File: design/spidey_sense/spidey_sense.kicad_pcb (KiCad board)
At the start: 2 copper layers, 63.5 x 46.5 mm, 14 parts, among them J1 Input_Screw_Terminal, J10 Output_Screw_Terminal, J2 Thermocouple_Terminal, J3 Thermocouple_Terminal, J4 Thermocouple_Terminal, J5 Thermocouple_Terminal, J6 Conn_01x06_Female, J7 Conn_01x06_Female, J8 Conn_01x06_Female, J9 Conn_01x06_Female

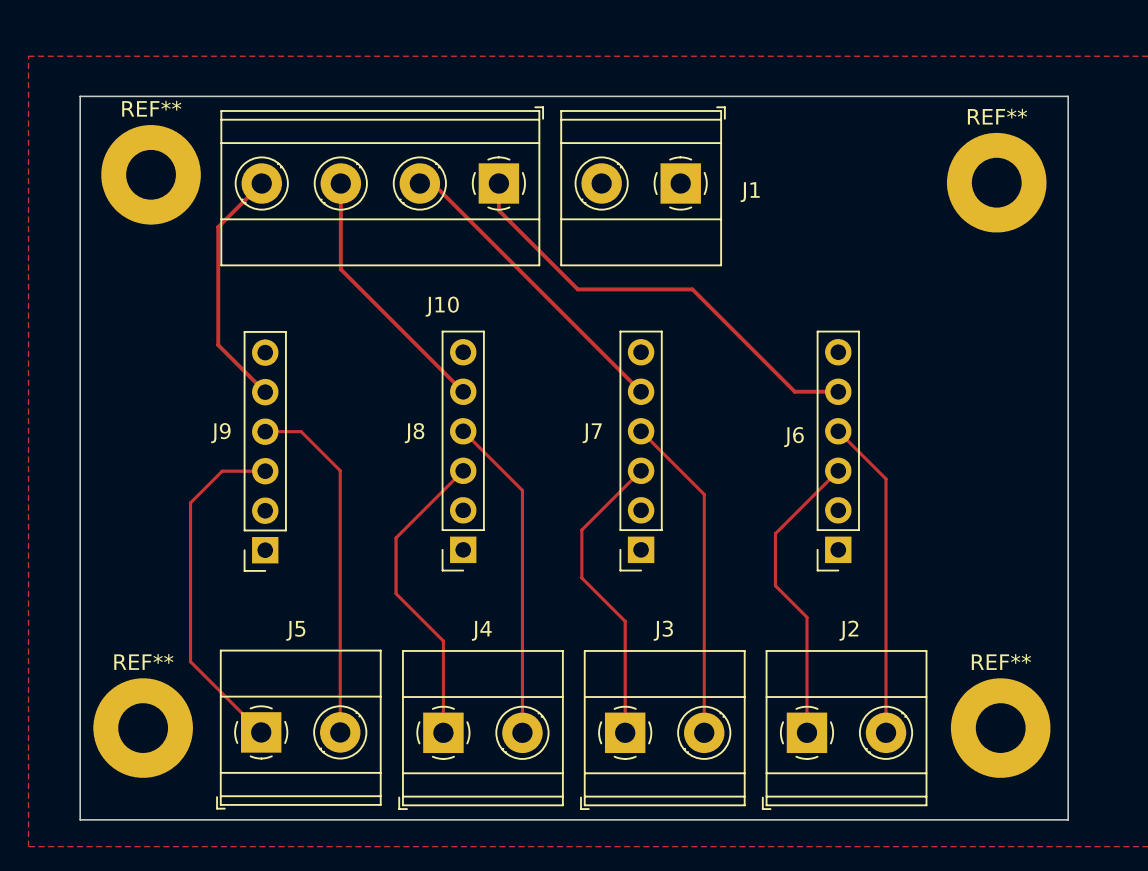
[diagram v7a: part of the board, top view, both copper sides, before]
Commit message: Routed all traces and set manufacturing constraints
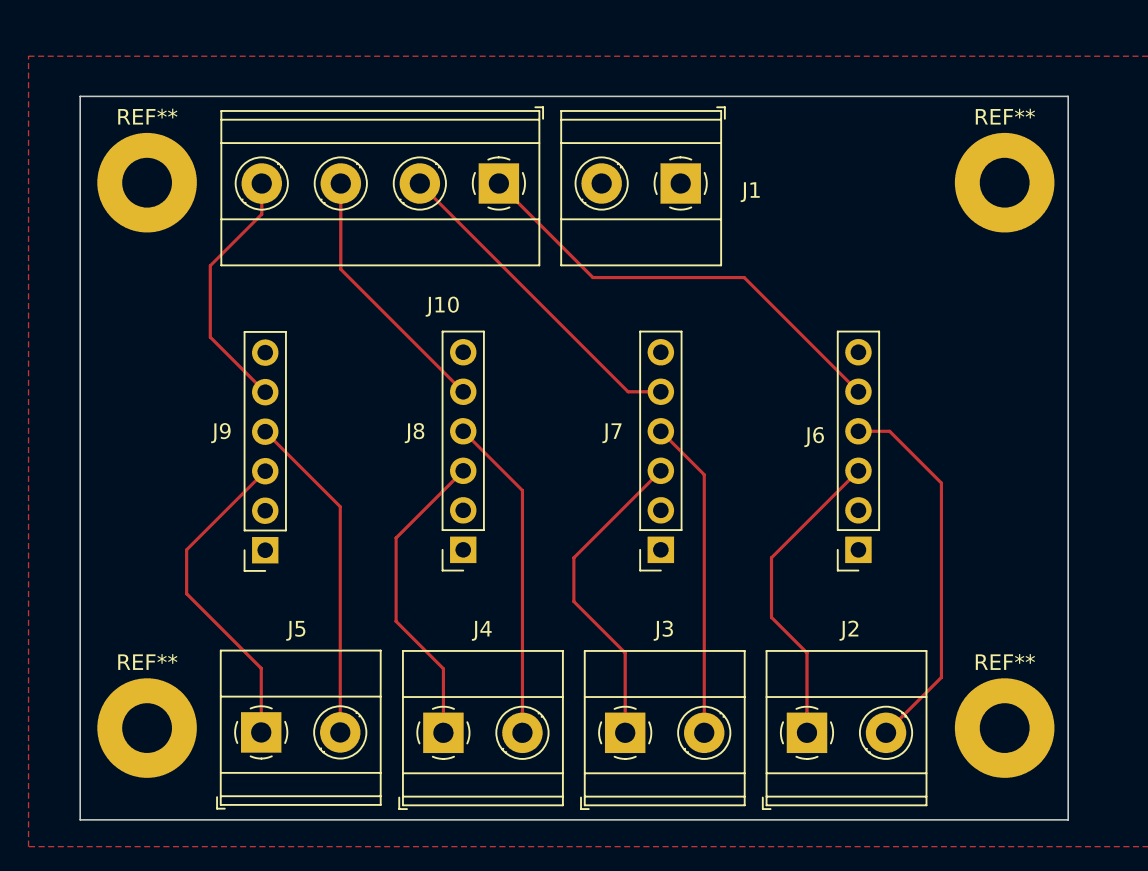
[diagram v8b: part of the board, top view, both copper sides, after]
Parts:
- moved J6 1.30 mm to (96.5, 90.1)
- moved J7 1.27 mm to (83.8, 90.1)
- moved REF** 0.57 mm to (50.8, 66.5)
- moved REF** 0.51 mm to (105.9, 66.5)
- moved REF** 0.25 mm to (105.9, 101.6)
- moved REF** 0.25 mm to (50.8, 101.6)
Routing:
- net /A-: track 20.7 -> 24.2 mm
- net /D+: track 22.3 -> 20.9 mm
- net /D-: track 22.7 -> 21.3 mm
- net /Bout: track 19.8 -> 21.0 mm
- net /B+: track 19.6 -> 20.5 mm
- net /A+: track 19.4 -> 20.1 mm
- net /B-: track 21.1 -> 20.5 mm
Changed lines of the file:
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@@
   )
   (setup
+    (stackup
+      (layer "F.SilkS" (type "Top Silk Screen"))
+      (layer "F.Paste" (type "Top Solder Paste"))
+      (layer "F.Mask" (type "Top Solder Mask") (thickness 0.01))
+      (layer "F.Cu" (type "copper") (thickness 0.035))
+      (layer "dielectric 1" (type "core") (thickness 1.51) (material "FR4") (epsilon_r 4.5) (loss_tangent 0.02))
+      (layer "B.Cu" (type "copper") (thickness 0.035))
+      (layer "B.Mask" (type "Bottom Solder Mask") (thickness 0.01))
+      (layer "B.Paste" (type "Bottom Solder Paste"))
+      (layer "B.SilkS" (type "Bottom Silk Screen"))
+      (copper_finish "None")
+      (dielectric_constraints no)
+    )
     (pad_to_mask_clearance 0)
     (pcbplotparams
@@
   (net 14 "/Dout")
   (footprint "Connector_PinSocket_2.54mm:PinSocket_1x06_P2.54mm_Vertical" (layer "F.Cu")
-    (at 82.55 90.145 180)
+    (at 83.82 90.145 180)
     (descr "Through hole straight socket strip, 1x06, 2.54mm pitch, single row (from Kicad 4.0.7), script generated")
     (tags "Through hole socket strip THT 1x06 2.54mm single row")
@@
   )
   (footprint "MountingHole:MountingHole_3.2mm_M3_Pad" (layer "F.Cu")
-    (at 105.41 66.548)
+    (at 105.918 66.548)
     (descr "Mounting Hole 3.2mm, M3")
     (tags "mounting hole 3.2mm m3")
@@
   )
   (footprint "MountingHole:MountingHole_3.2mm_M3_Pad" (layer "F.Cu")
-    (at 50.546 101.6)
+    (at 50.8 101.6)
     (descr "Mounting Hole 3.2mm, M3")
     (tags "mounting hole 3.2mm m3")
@@
   )
   (footprint "Connector_PinSocket_2.54mm:PinSocket_1x06_P2.54mm_Vertical" (layer "F.Cu")
-    (at 95.225 90.145 180)
+    (at 96.52 90.145 180)
     (descr "Through hole straight socket strip, 1x06, 2.54mm pitch, single row (from Kicad 4.0.7), script generated")
     (tags "Through hole socket strip THT 1x06 2.54mm single row")
@@
   )
   (footprint "MountingHole:MountingHole_3.2mm_M3_Pad" (layer "F.Cu")
-    (at 105.664 101.6)
+    (at 105.918 101.6)
     (descr "Mounting Hole 3.2mm, M3")
     (tags "mounting hole 3.2mm m3")
@@
   )
   (footprint "MountingHole:MountingHole_3.2mm_M3_Pad" (layer "F.Cu")
-    (at 51.054 66.04)
+    (at 50.8 66.548)
     (descr "Mounting Hole 3.2mm, M3")
     (tags "mounting hole 3.2mm m3")
@@
     (style (thickness 0.15) (arrow_length 1.27) (text_position_mode 0) (extension_height 0.58642) (extension_offset 0.5) keep_text_aligned)
   )
-  (segment (start 93.213 94.483) (end 91.186 92.456) (width 0.2) (layer "F.Cu") (net 3))
-  (segment (start 91.186 89.104) (end 95.225 85.065) (width 0.2) (layer "F.Cu") (net 3))
-  (segment (start 93.213 101.905) (end 93.213 94.483) (width 0.2) (layer "F.Cu") (net 3))
-  (segment (start 91.186 92.456) (end 91.186 89.104) (width 0.2) (layer "F.Cu") (net 3))
-  (segment (start 98.293 85.593) (end 95.225 82.525) (width 0.2) (layer "F.Cu") (net 4))
-  (segment (start 98.293 101.905) (end 98.293 85.593) (width 0.2) (layer "F.Cu") (net 4))
-  (segment (start 78.74 88.875) (end 82.55 85.065) (width 0.2) (layer "F.Cu") (net 5))
-  (segment (start 78.74 91.948) (end 78.74 88.875) (width 0.2) (layer "F.Cu") (net 5))
-  (segment (start 81.529 94.737) (end 78.74 91.948) (width 0.2) (layer "F.Cu") (net 5))
-  (segment (start 81.529 101.905) (end 81.529 94.737) (width 0.2) (layer "F.Cu") (net 5))
-  (segment (start 86.609 86.584) (end 82.55 82.525) (width 0.2) (layer "F.Cu") (net 6))
-  (segment (start 86.609 101.905) (end 86.609 86.584) (width 0.2) (layer "F.Cu") (net 6))
-  (segment (start 69.845 101.905) (end 69.845 96.007) (width 0.2) (layer "F.Cu") (net 7))
-  (segment (start 66.802 89.383) (end 71.12 85.065) (width 0.2) (layer "F.Cu") (net 7))
-  (segment (start 69.845 96.007) (end 66.802 92.964) (width 0.2) (layer "F.Cu") (net 7))
-  (segment (start 66.802 92.964) (end 66.802 89.383) (width 0.2) (layer "F.Cu") (net 7))
-  (segment (start 74.925 101.905) (end 74.925 86.33) (width 0.2) (layer "F.Cu") (net 8))
-  (segment (start 74.925 86.33) (end 71.12 82.525) (width 0.2) (layer "F.Cu") (net 8))
-  (segment (start 55.626 85.09) (end 53.594 87.122) (width 0.2) (layer "F.Cu") (net 9))
-  (segment (start 58.395 85.09) (end 55.626 85.09) (width 0.2) (layer "F.Cu") (net 9))
-  (segment (start 53.594 87.122) (end 53.594 97.338) (width 0.2) (layer "F.Cu") (net 9))
-  (segment (start 53.594 97.338) (end 58.1356 101.8796) (width 0.2) (layer "F.Cu") (net 9))
-  (segment (start 63.2156 85.0596) (end 63.2156 101.8796) (width 0.2) (layer "F.Cu") (net 10))
-  (segment (start 60.706 82.55) (end 63.2156 85.0596) (width 0.2) (layer "F.Cu") (net 10))
-  (segment (start 58.395 82.55) (end 60.706 82.55) (width 0.2) (layer "F.Cu") (net 10))
-  (segment (start 73.411 68.331) (end 73.411 66.6) (width 0.25) (layer "F.Cu") (net 11))
-  (segment (start 95.225 79.985) (end 92.431 79.985) (width 0.25) (layer "F.Cu") (net 11))
-  (segment (start 92.431 79.985) (end 85.852 73.406) (width 0.25) (layer "F.Cu") (net 11))
-  (segment (start 85.852 73.406) (end 78.486 73.406) (width 0.25) (layer "F.Cu") (net 11))
-  (segment (start 78.486 73.406) (end 73.411 68.331) (width 0.25) (layer "F.Cu") (net 11))
-  (segment (start 82.55 79.985) (end 69.165 66.6) (width 0.25) (layer "F.Cu") (net 12))
-  (segment (start 69.165 66.6) (end 68.331 66.6) (width 0.25) (layer "F.Cu") (net 12))
-  (segment (start 63.251 72.116) (end 63.251 66.6) (width 0.25) (layer "F.Cu") (net 13))
-  (segment (start 71.12 79.985) (end 63.251 72.116) (width 0.25) (layer "F.Cu") (net 13))
-  (segment (start 55.372 76.987) (end 55.372 69.399) (width 0.25) (layer "F.Cu") (net 14))
-  (segment (start 58.395 80.01) (end 55.372 76.987) (width 0.25) (layer "F.Cu") (net 14))
-  (segment (start 55.372 69.399) (end 58.171 66.6) (width 0.25) (layer "F.Cu") (net 14))
+  (segment (start 90.932 94.488) (end 90.932 90.653) (width 0.2032) (layer "F.Cu") (net 3))
+  (segment (start 93.213 96.769) (end 90.932 94.488) (width 0.2032) (layer "F.Cu") (net 3))
+  (segment (start 90.932 90.653) (end 96.52 85.065) (width 0.2032) (layer "F.Cu") (net 3))
+  (segment (start 93.213 101.905) (end 93.213 96.769) (width 0.2032) (layer "F.Cu") (net 3))
+  (segment (start 101.854 85.852) (end 98.527 82.525) (width 0.2032) (layer "F.Cu") (net 4))
+  (segment (start 101.854 98.344) (end 101.854 85.852) (width 0.2032) (layer "F.Cu") (net 4))
+  (segment (start 98.527 82.525) (end 96.52 82.525) (width 0.2032) (layer "F.Cu") (net 4))
+  (segment (start 98.293 101.905) (end 101.854 98.344) (width 0.2032) (layer "F.Cu") (net 4))
+  (segment (start 78.232 90.653) (end 83.82 85.065) (width 0.2032) (layer "F.Cu") (net 5))
+  (segment (start 81.529 96.769) (end 78.232 93.472) (width 0.2032) (layer "F.Cu") (net 5))
+  (segment (start 81.529 101.905) (end 81.529 96.769) (width 0.2032) (layer "F.Cu") (net 5))
+  (segment (start 78.232 93.472) (end 78.232 90.653) (width 0.2032) (layer "F.Cu") (net 5))
+  (segment (start 86.609 101.905) (end 86.609 85.314) (width 0.2032) (layer "F.Cu") (net 6))
+  (segment (start 86.609 85.314) (end 83.82 82.525) (width 0.2032) (layer "F.Cu") (net 6))
+  (segment (start 66.802 94.742) (end 66.802 89.383) (width 0.2032) (layer "F.Cu") (net 7))
+  (segment (start 66.802 89.383) (end 71.12 85.065) (width 0.2032) (layer "F.Cu") (net 7))
+  (segment (start 69.845 97.785) (end 66.802 94.742) (width 0.2032) (layer "F.Cu") (net 7))
+  (segment (start 69.845 101.905) (end 69.845 97.785) (width 0.2032) (layer "F.Cu") (net 7))
+  (segment (start 74.925 101.905) (end 74.925 86.33) (width 0.2032) (layer "F.Cu") (net 8))
+  (segment (start 74.925 86.33) (end 71.12 82.525) (width 0.2032) (layer "F.Cu") (net 8))
+  (segment (start 58.1356 101.8796) (end 58.1356 97.7596) (width 0.2032) (layer "F.Cu") (net 9))
+  (segment (start 53.34 92.964) (end 53.34 90.145) (width 0.2032) (layer "F.Cu") (net 9))
+  (segment (start 58.1356 97.7596) (end 53.34 92.964) (width 0.2032) (layer "F.Cu") (net 9))
+  (segment (start 53.34 90.145) (end 58.395 85.09) (width 0.2032) (layer "F.Cu") (net 9))
+  (segment (start 63.2156 87.3706) (end 58.395 82.55) (width 0.2032) (layer "F.Cu") (net 10))
+  (segment (start 63.2156 101.8796) (end 63.2156 87.3706) (width 0.2032) (layer "F.Cu") (net 10))
+  (segment (start 89.179 72.644) (end 96.52 79.985) (width 0.2032) (layer "F.Cu") (net 11))
+  (segment (start 79.455 72.644) (end 89.179 72.644) (width 0.2032) (layer "F.Cu") (net 11))
+  (segment (start 73.411 66.6) (end 79.455 72.644) (width 0.2032) (layer "F.Cu") (net 11))
+  (segment (start 68.331 66.6) (end 81.716 79.985) (width 0.2032) (layer "F.Cu") (net 12))
+  (segment (start 81.716 79.985) (end 83.82 79.985) (width 0.2032) (layer "F.Cu") (net 12))
+  (segment (start 63.251 72.116) (end 71.12 79.985) (width 0.2032) (layer "F.Cu") (net 13))
+  (segment (start 63.251 66.6) (end 63.251 72.116) (width 0.2032) (layer "F.Cu") (net 13))
+  (segment (start 58.171 68.575) (end 54.864 71.882) (width 0.2032) (layer "F.Cu") (net 14))
+  (segment (start 54.864 71.882) (end 54.864 76.479) (width 0.2032) (layer "F.Cu") (net 14))
+  (segment (start 58.171 66.6) (end 58.171 68.575) (width 0.2032) (layer "F.Cu") (net 14))
+  (segment (start 54.864 76.479) (end 58.395 80.01) (width 0.2032) (layer "F.Cu") (net 14))
   (zone (net 2) (net_name "+24V") (layer "F.Cu") (hatch edge 0.508)
     (connect_pads (clearance 0.508))
